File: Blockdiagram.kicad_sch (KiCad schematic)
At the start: 0 parts

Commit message: Added interconnect between CPU and PCH boards and added ATX board outline
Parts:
- added H1: ATX_A, MountingHole:MountingHole_4.3mm_M4_Pad_Via, symbol Mechanical:MountingHole_Pad
- added H2: ATX_C, MountingHole:MountingHole_4.3mm_M4_Pad_Via, symbol Mechanical:MountingHole_Pad
- added H3: ATX_F, MountingHole:MountingHole_4.3mm_M4_Pad_Via, symbol Mechanical:MountingHole_Pad
- added H4: ATX_G, MountingHole:MountingHole_4.3mm_M4_Pad_Via, symbol Mechanical:MountingHole_Pad
- added H5: ATX_H, MountingHole:MountingHole_4.3mm_M4_Pad_Via, symbol Mechanical:MountingHole_Pad
- added H6: ATX_J, MountingHole:MountingHole_4.3mm_M4_Pad_Via, symbol Mechanical:MountingHole_Pad
- added H7: ATX_K, MountingHole:MountingHole_4.3mm_M4_Pad_Via, symbol Mechanical:MountingHole_Pad
- added H8: ATX_L, MountingHole:MountingHole_4.3mm_M4_Pad_Via, symbol Mechanical:MountingHole_Pad
- added H9: ATX_M, MountingHole:MountingHole_4.3mm_M4_Pad_Via, symbol Mechanical:MountingHole_Pad
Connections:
- new net GND: H1.1, H2.1, H3.1, H4.1, H5.1, H6.1, H7.1, H8.1, H9.1

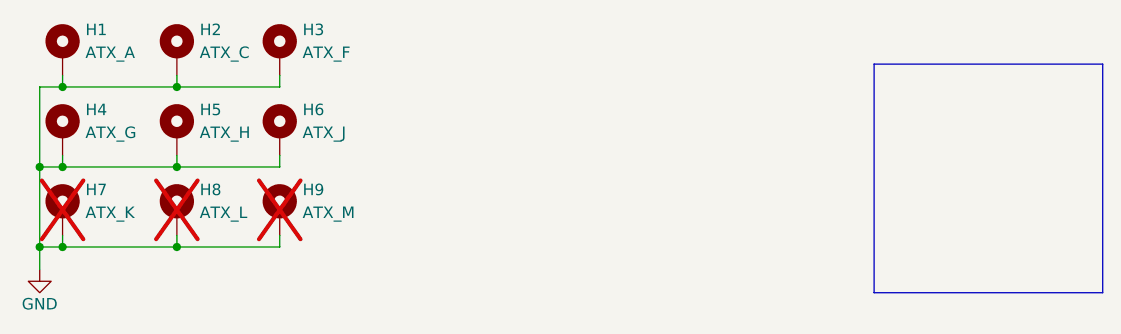
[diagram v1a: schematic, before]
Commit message: Added more PCIe slots and mounting holes
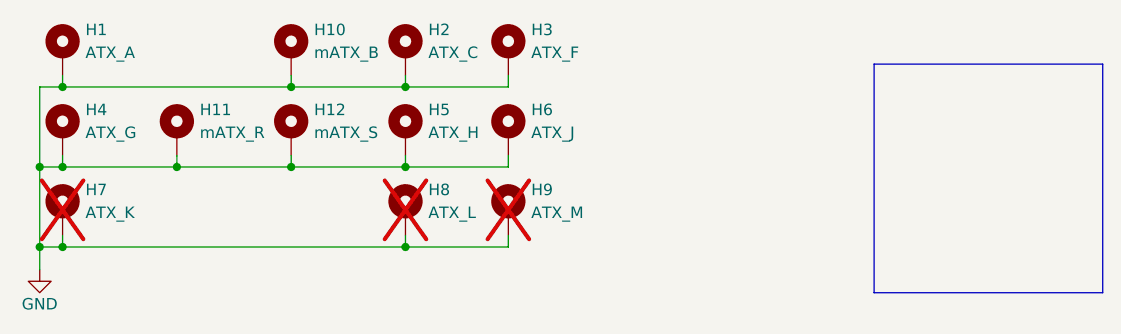
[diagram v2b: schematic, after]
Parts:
- added H10: mATX_B, MountingHole:MountingHole_4.3mm_M4_Pad_Via, symbol Mechanical:MountingHole_Pad
- added H11: mATX_R, MountingHole:MountingHole_4.3mm_M4_Pad_Via, symbol Mechanical:MountingHole_Pad
- added H12: mATX_S, MountingHole:MountingHole_4.3mm_M4_Pad_Via, symbol Mechanical:MountingHole_Pad
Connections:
- net GND: now also H10.1, H11.1, H12.1
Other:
- moved on the sheet: H2, H3, H5, H6, H8, H9
